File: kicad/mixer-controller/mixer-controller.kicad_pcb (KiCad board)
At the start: 2 copper layers, 73.8 x 67.9 mm, 20 parts, among them J1 RS485, J2 CAN, J3 ADC, J4 PWR_IN, J5 CAN, U2 AP1117-50, U3 TJA1050, U4 ESP32-DEVKITC-32U

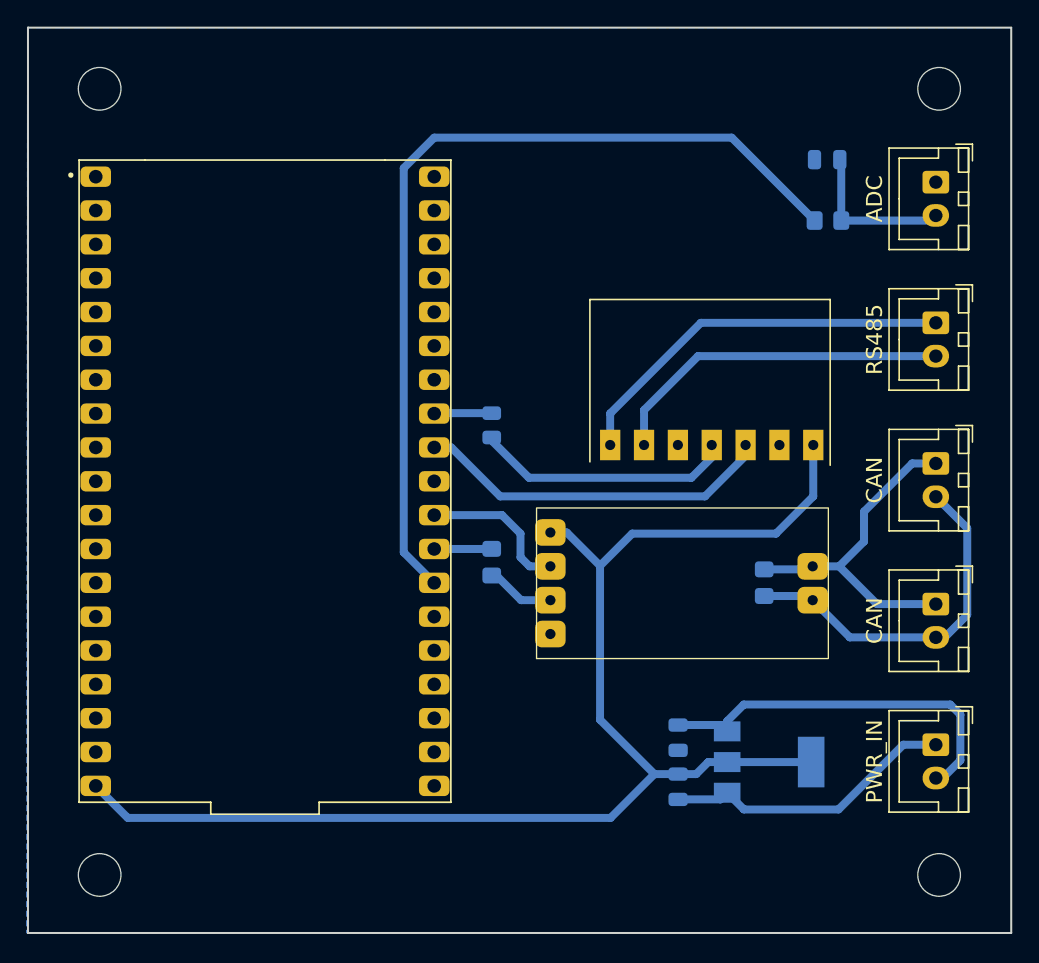
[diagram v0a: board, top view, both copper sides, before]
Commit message: Added encoder breakout and updated other projects
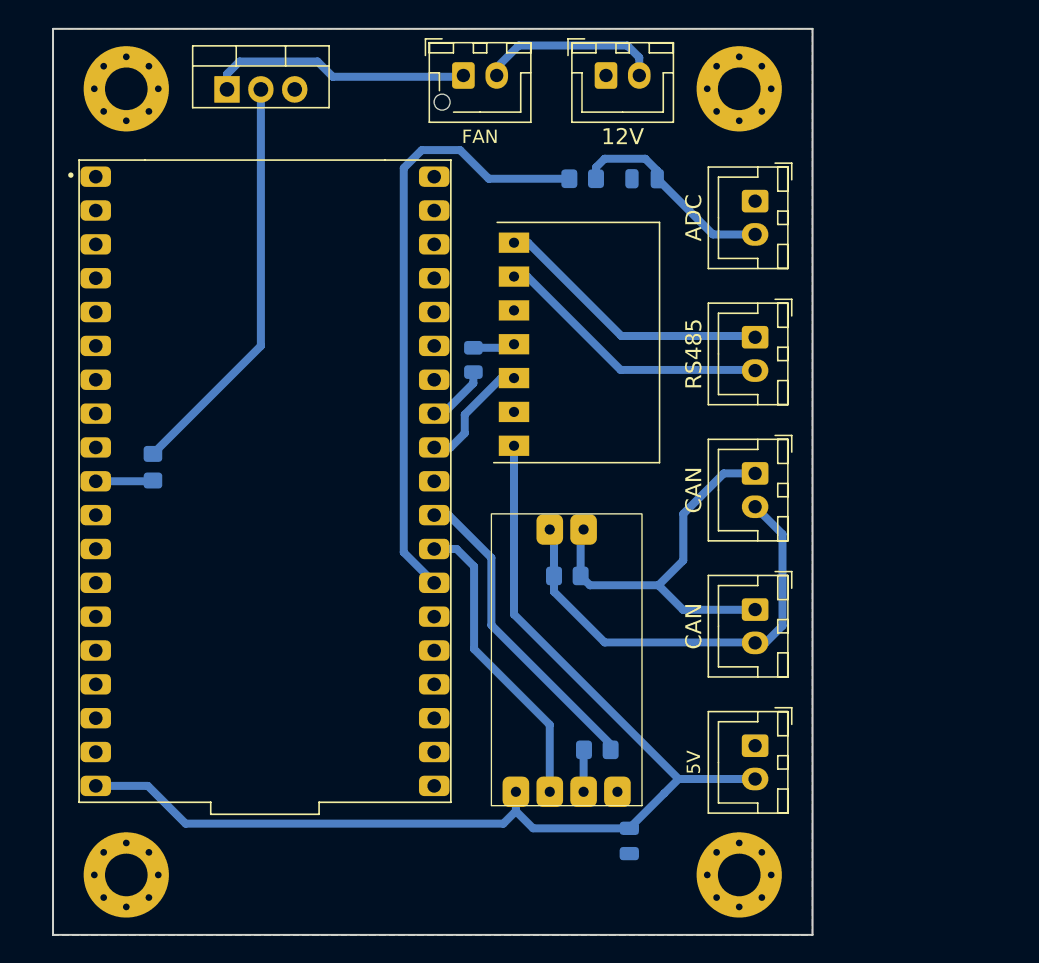
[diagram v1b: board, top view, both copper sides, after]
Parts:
- removed C1: 10u, Capacitor_SMD:C_0805_2012Metric
- removed U2: AP1117-50, Package_TO_SOT_SMD:SOT-223-3_TabPin2
- added J6: FAN, Connector_JST:JST_XH_B2B-XH-AM_1x02_P2.50mm_Vertical, F.Cu at (104.3, 45.5)
- added J7: 5V, Connector_JST:JST_XH_B2B-XH-A_1x02_P2.50mm_Vertical, F.Cu at (126.2, 95.8)
- added Q1: NCEP60T20, Package_TO_SOT_THT:TO-220-3_Vertical, F.Cu at (86.6, 46.5)
- added R5: 1k, Resistor_SMD:R_0805_2012Metric_Pad1.20x1.40mm_HandSolder, B.Cu at (81.0, 74.9)
- H1, H2, H3, H4: footprint MountingHole:MountingHole_3.2mm_M3 -> MountingHole:MountingHole_3.2mm_M3_Pad_Via
- J4: value PWR_IN -> 12V
- moved J4 56.0 mm to (115.0, 45.5), turned to 0 degrees
- moved R3 18.7 mm to (113.2, 53.2)
- moved CU1 17.0 mm to (118.5, 74.1), turned to 180 degrees
- moved R2 16.2 mm to (114.3, 96.1), turned to 0 degrees
- moved U3 15.6 mm to (118.4, 101.8), turned to 180 degrees
- moved H3 15.0 mm to (125.0, 46.5)
- moved H4 15.0 mm to (125.0, 105.5)
- moved R4 14.8 mm to (112.1, 83.1), turned to 180 degrees
- moved C3 13.8 mm to (117.9, 53.2)
- moved J3 13.6 mm to (126.2, 54.9)
- moved J1 13.6 mm to (126.2, 65.1)
- moved J5 13.6 mm to (126.2, 75.4)
- moved J2 13.6 mm to (126.2, 85.6)
- moved C2 5.47 mm to (116.8, 103.0)
- moved R1 5.09 mm to (105.0, 66.8), turned to 90 degrees
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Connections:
- J2 pad 1: /CAN_H -> /CAN_L
- J2 pad 2: /CAN_L -> /CAN_H
- J5 pad 1: /CAN_H -> /CAN_L
- J5 pad 2: /CAN_L -> /CAN_H
- U4 pad 10: unconnected-(U4-IO26-Pad10) -> /ESP_GPIO_FAN
- U4 pad 27: /ESP_CAN_RX -> /ESP_CAN_TX
- U4 pad 28: /ESP_CAN_TX -> /ESP_CAN_RX
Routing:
- net Net-(Q1-G): track 0.00 -> 30.7 mm
- net GND: track 21.9 -> 0.00 mm
- net /ESP_MOTOR_PWM: track 66.4 -> 46.0 mm
- net Net-(J6-Pin_1): track 0.00 -> 19.8 mm
- net /ESP_CAN_RX: track 4.32 -> 23.7 mm
- net /ESP_MODBUS_TX: track 27.0 -> 8.97 mm
- net Net-(CU1-RXD): track 19.5 -> 3.16 mm
- net +5V: track 100.5 -> 84.7 mm
- net +12V: track 29.0 -> 13.7 mm
- net /ESP_CAN_TX: track 11.4 -> 22.8 mm
- net /IN_B: track 29.6 -> 21.0 mm
- net /CAN_H: track 26.2 -> 33.9 mm
- net /IN_A: track 26.2 -> 21.0 mm
- net /ESP_GPIO_FAN: track 0.00 -> 4.32 mm
- net Net-(J3-Pin_2): track 11.9 -> 15.8 mm
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- added copper zone on F.Cu, net GND
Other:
- board size 73.8 x 67.9 mm -> 57 x 68 mm

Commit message: Final updates for manufacturing
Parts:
- J6: footprint Connector_JST:JST_XH_B2B-XH-AM_1x02_P2.50mm_Vertical -> Connector_JST:JST_XH_B2B-XH-A_1x02_P2.50mm_Vertical
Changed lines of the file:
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@@
     (pad "1" thru_hole circle (at 2.4 0) (size 0.8 0.8) (drill 0.5) (layers "*.Cu" "*.Mask"))
   )
-  (footprint "Connector_JST:JST_XH_B2B-XH-AM_1x02_P2.50mm_Vertical" (layer "F.Cu")
+  (footprint "Connector_JST:JST_XH_B2B-XH-A_1x02_P2.50mm_Vertical" (layer "F.Cu")
     (at 104.3 45.5)
-    (descr "JST XH series connector, B2B-XH-AM, with boss (http://www.jst-mfg.com/product/pdf/eng/eXH.pdf), generated with kicad-footprint-generator")
-    (tags "connector JST XH vertical boss")
+    (descr "JST XH series connector, B2B-XH-A (http://www.jst-mfg.com/product/pdf/eng/eXH.pdf), generated with kicad-footprint-generator")
+    (tags "connector JST XH vertical")
     (property "Sheetfile" "mixer-controller.kicad_sch")
     (property "Sheetname" "")
@@
         (effects (font (size 1 1) (thickness 0.15)))
     )
-    (fp_text value "FAN" (at 1.25 4.6) (layer "F.SilkS")
+    (fp_text value "FAN" (at 1.25 4.6) (layer "F.Fab")
         (effects (font (size 1 1) (thickness 0.15)))
     )
@@
     (fp_line (start -2.55 -0.2) (end -1.8 -0.2)
       (stroke (width 0.12) (type solid)) (layer "F.SilkS"))
-    (fp_line (start -1.8 -0.2) (end -1.8 1.14)
+    (fp_line (start -1.8 -0.2) (end -1.8 2.75)
+      (stroke (width 0.12) (type solid)) (layer "F.SilkS"))
+    (fp_line (start -1.8 2.75) (end 1.25 2.75)
       (stroke (width 0.12) (type solid)) (layer "F.SilkS"))
     (fp_line (start -1.6 -2.75) (end -2.85 -2.75)
@@
       (stroke (width 0.12) (type solid)) (layer "F.SilkS"))
     (fp_line (start 0.75 -1.7) (end 1.75 -1.7)
-      (stroke (width 0.12) (type solid)) (layer "F.SilkS"))
-    (fp_line (start 1.25 2.75) (end -0.74 2.75)
       (stroke (width 0.12) (type solid)) (layer "F.SilkS"))
     (fp_line (start 1.75 -2.45) (end 0.75 -2.45)
@@
     (fp_line (start 4.95 3.4) (end 4.95 -2.35)
       (stroke (width 0.1) (type solid)) (layer "F.Fab"))
-    (pad "" np_thru_hole circle (at -1.6 2) (size 1.2 1.2) (drill 1.2) (layers "*.Cu" "*.Mask"))
     (pad "1" thru_hole roundrect (at 0 0) (size 1.7 2) (drill 1) (layers "*.Cu" "*.Mask") (roundrect_rratio 0.147059)
       (net 44 "Net-(J6-Pin_1)") (pinfunction "Pin_1") (pintype "passive"))
     (pad "2" thru_hole oval (at 2.5 0) (size 1.7 2) (drill 1) (layers "*.Cu" "*.Mask")
       (net 3 "+12V") (pinfunction "Pin_2") (pintype "passive"))
-    (model "${KICAD6_3DMODEL_DIR}/Connector_JST.3dshapes/JST_XH_B2B-XH-AM_1x02_P2.50mm_Vertical.wrl"
+    (model "${KICAD6_3DMODEL_DIR}/Connector_JST.3dshapes/JST_XH_B2B-XH-A_1x02_P2.50mm_Vertical.wrl"
       (offset (xyz 0 0 0))
       (scale (xyz 1 1 1))
@@
     (property "ki_keywords" "R res resistor")
     (attr smd)
-    (fp_text reference "R2" (at 0 1.65) (layer "B.SilkS") hide
+    (fp_text reference "R2" (at 0 -1.66) (layer "B.SilkS")
         (effects (font (size 1 1) (thickness 0.15)) (justify mirror))
     )
@@
     (property "ki_keywords" "R res resistor")
     (attr smd)
-    (fp_text reference "R4" (at 0 1.65) (layer "B.SilkS")
+    (fp_text reference "R4" (at -0.1 -1.69) (layer "B.SilkS")
         (effects (font (size 1 1) (thickness 0.15)) (justify mirror))
     )
@@
     (property "ki_keywords" "R res resistor")
     (attr smd)
-    (fp_text reference "R1" (at 0 1.65 90) (layer "B.SilkS") hide
+    (fp_text reference "R1" (at 2.7 0.05 180) (layer "B.SilkS")
         (effects (font (size 1 1) (thickness 0.15)) (justify mirror))
     )
@@
     (property "ki_keywords" "cap capacitor")
     (attr smd)
-    (fp_text reference "C2" (at 0 1.68 90) (layer "B.SilkS") hide
+    (fp_text reference "C2" (at 2.55 -0.1 -180) (layer "B.SilkS")
         (effects (font (size 1 1) (thickness 0.15)) (justify mirror))
     )
@@
     (property "ki_keywords" "R res resistor")
     (attr smd)
-    (fp_text reference "R5" (at 0 1.65 90) (layer "B.SilkS")
-        (effects (font (size 1 1) (thickness 0.15)) (justify mirror))
-    )
+    (fp_text reference "R5" (at 2.85 0 -180) (layer "B.SilkS")
+        (effects (font (size 1 1) (thickness 0.15)) (justify mirror))
+    )
